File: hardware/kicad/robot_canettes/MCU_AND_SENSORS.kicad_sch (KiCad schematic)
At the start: 28 parts, among them J9 Conn_01x04_Pin, U1 STM32G431RBTx, U6 SN74AHCT1G125DBVR, Y1 16M

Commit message: Mise à jour de l'emplacement des composants
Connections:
- net GND: now also C1.2, C10.2, C15.2, C16.2, C17.2, C2.2, C22.2, C23.1, C3.2, C4.2, C5.2, C6.2, C7.2, C8.2, C9.2, H101.1, H102.1, H103.1, H104.1, J9.3 (Pin_3), LCSC1.11 (GNDDetect), LCSC1.5 (GND), LCSC1.7 (GND), R1.2, SW2.1, U1.15 (VSS), U1.27 (VSSA), U1.31 (VSS), U1.47 (VSS), U1.63 (VSS), Y1.2 (G), Y1.4 (G)
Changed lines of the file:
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@@
 			)
 		)
-		(property "Value" ""
+		(property "Value" "GND"
 			(at 52.07 91.44 0)
+			(hide yes)
 			(show_name no)
 			(do_not_autoplace no)
@@
 			)
 		)
-		(property "Value" ""
+		(property "Value" "GND"
 			(at 60.96 86.36 0)
+			(hide yes)
 			(show_name no)
 			(do_not_autoplace no)
@@
 			)
 		)
-		(property "Value" ""
+		(property "Value" "GND"
 			(at 113.03 166.37 0)
+			(hide yes)
 			(show_name no)
 			(do_not_autoplace no)
@@
 			)
 		)
-		(property "Value" ""
+		(property "Value" "GND"
 			(at 71.12 62.23 0)
+			(hide yes)
 			(show_name no)
 			(do_not_autoplace no)
@@
 			)
 		)
-		(property "Value" ""
+		(property "Value" "GND"
 			(at 248.92 52.07 0)
+			(hide yes)
 			(show_name no)
 			(do_not_autoplace no)
@@
 			)
 		)
-		(property "Value" ""
+		(property "Value" "GND"
 			(at 252.73 137.16 0)
+			(hide yes)
 			(show_name no)
 			(do_not_autoplace no)
@@
 			)
 		)
-		(property "Value" ""
+		(property "Value" "GND"
 			(at 64.77 101.6 0)
+			(hide yes)
 			(show_name no)
 			(do_not_autoplace no)
@@
 			)
 		)
-		(property "Value" ""
+		(property "Value" "GND"
 			(at 149.86 146.05 0)
+			(hide yes)
 			(show_name no)
 			(do_not_autoplace no)
@@
 			)
 		)
-		(property "Value" ""
+		(property "Value" "GND"
 			(at 52.07 181.61 0)
+			(hide yes)
 			(show_name no)
 			(do_not_autoplace no)
@@
 			)
 		)
-		(property "Value" ""
+		(property "Value" "GND"
 			(at 233.68 83.82 0)
+			(hide yes)
 			(show_name no)
 			(do_not_autoplace no)
@@
 			)
 		)
-		(property "Value" ""
+		(property "Value" "GND"
 			(at 243.84 137.16 0)
+			(hide yes)
 			(show_name no)
 			(do_not_autoplace no)
@@
 			)
 		)
-		(property "Value" ""
+		(property "Value" "GND"
 			(at 147.32 57.15 0)
+			(hide yes)
 			(show_name no)
 			(do_not_autoplace no)
@@
 			)
 		)
-		(property "Value" ""
+		(property "Value" "GND"
 			(at 45.72 80.01 0)
+			(hide yes)
 			(show_name no)
 			(do_not_autoplace no)

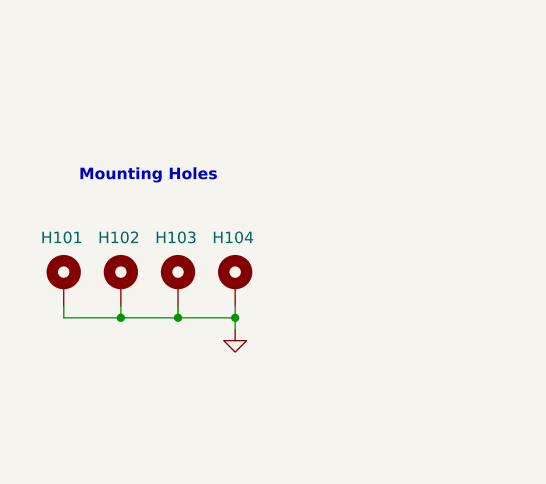
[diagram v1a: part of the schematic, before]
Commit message: Mise à jour PCB depuis le zip
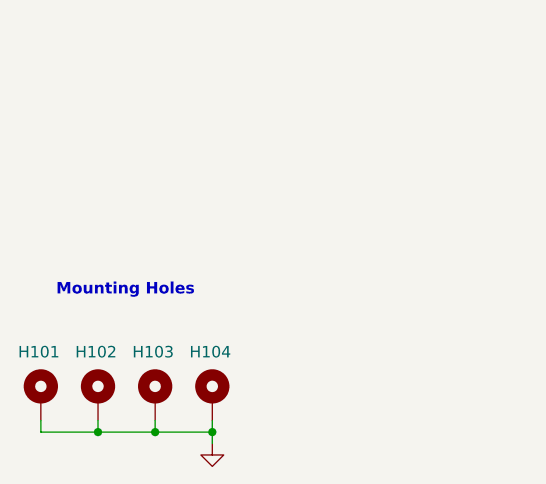
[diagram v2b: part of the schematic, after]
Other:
- moved on the sheet: H101, H102, H103, H104
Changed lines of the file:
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@@
 	(text "Mounting Holes"
 		(exclude_from_sim no)
-		(at 42.418 160.782 0)
+		(at 39.878 173.482 0)
 		(effects
 			(font
@@
 	)
 	(junction
-		(at 52.07 176.53)
+		(at 49.53 189.23)
 		(diameter 0)
 		(color 0 0 0 0)
 	)
 	(junction
-		(at 39.37 176.53)
+		(at 36.83 189.23)
 		(diameter 0)
 		(color 0 0 0 0)
@@
 	)
 	(junction
-		(at 45.72 176.53)
+		(at 43.18 189.23)
 		(diameter 0)
 		(color 0 0 0 0)
@@
 	(wire
 		(pts
-			(xy 45.72 176.53) (xy 39.37 176.53)
+			(xy 43.18 189.23) (xy 36.83 189.23)
 		)
 		(stroke
@@
 	(wire
 		(pts
-			(xy 33.02 176.53) (xy 33.02 175.26)
+			(xy 30.48 189.23) (xy 30.48 187.96)
 		)
 		(stroke
@@
 	(wire
 		(pts
-			(xy 39.37 176.53) (xy 39.37 175.26)
+			(xy 36.83 189.23) (xy 36.83 187.96)
 		)
 		(stroke
@@
 	(wire
 		(pts
-			(xy 39.37 176.53) (xy 33.02 176.53)
+			(xy 36.83 189.23) (xy 30.48 189.23)
 		)
 		(stroke
@@
 	(wire
 		(pts
-			(xy 52.07 176.53) (xy 52.07 177.8)
+			(xy 49.53 189.23) (xy 49.53 190.5)
 		)
 		(stroke
@@
 	(wire
 		(pts
-			(xy 52.07 175.26) (xy 52.07 176.53)
+			(xy 49.53 187.96) (xy 49.53 189.23)
 		)
 		(stroke
@@
 	(wire
 		(pts
-			(xy 52.07 176.53) (xy 45.72 176.53)
+			(xy 49.53 189.23) (xy 43.18 189.23)
 		)
 		(stroke
@@
 	(wire
 		(pts
-			(xy 45.72 176.53) (xy 45.72 175.26)
+			(xy 43.18 189.23) (xy 43.18 187.96)
 		)
 		(stroke
@@
 	(symbol
 		(lib_id "Mechanical:MountingHole_Pad")
-		(at 33.02 172.72 0)
+		(at 30.48 185.42 0)
 		(unit 1)
 		(body_style 1)
@@
 		(dnp no)
 		(property "Reference" "H101"
-			(at 30.48 167.64 0)
+			(at 27.94 180.34 0)
 			(show_name no)
 			(do_not_autoplace no)
@@
 		)
 		(property "Value" "MountingHole_Pad"
-			(at 35.56 172.72 0)
+			(at 33.02 185.42 0)
 			(hide yes)
 			(show_name no)
@@
 		)
 		(property "Footprint" "MountingHole:MountingHole_3.2mm_M3_Pad_Via"
-			(at 33.02 172.72 0)
+			(at 30.48 185.42 0)
 			(hide yes)
 			(show_name no)
@@
 		)
 		(property "Datasheet" ""
-			(at 33.02 172.72 0)
+			(at 30.48 185.42 0)
 			(hide yes)
 			(show_name no)
@@
 		)
 		(property "Description" ""
-			(at 33.02 172.72 0)
+			(at 30.48 185.42 0)
 			(show_name no)
 			(do_not_autoplace no)
@@
 	(symbol
 		(lib_id "Mechanical:MountingHole_Pad")
-		(at 39.37 172.72 0)
+		(at 36.83 185.42 0)
 		(unit 1)
 		(body_style 1)
@@
 		(dnp no)
 		(property "Reference" "H102"
-			(at 36.83 167.64 0)
+			(at 34.29 180.34 0)
 			(show_name no)
 			(do_not_autoplace no)
@@
 		)
 		(property "Value" "MountingHole_Pad"
-			(at 41.91 172.72 0)
+			(at 39.37 185.42 0)
 			(hide yes)
 			(show_name no)
@@
 		)
 		(property "Footprint" "MountingHole:MountingHole_3.2mm_M3_Pad_Via"
-			(at 39.37 172.72 0)
+			(at 36.83 185.42 0)
 			(hide yes)
 			(show_name no)
@@
 		)
 		(property "Datasheet" ""
-			(at 39.37 172.72 0)
+			(at 36.83 185.42 0)
 			(hide yes)
 			(show_name no)
@@
 		)
 		(property "Description" ""
-			(at 39.37 172.72 0)
+			(at 36.83 185.42 0)
 			(show_name no)
 			(do_not_autoplace no)
@@
 	(symbol
 		(lib_id "Mechanical:MountingHole_Pad")
-		(at 45.72 172.72 0)
+		(at 43.18 185.42 0)
 		(unit 1)
 		(body_style 1)
@@
 		(dnp no)
 		(property "Reference" "H103"
-			(at 43.18 167.64 0)
+			(at 40.64 180.34 0)
 			(show_name no)
 			(do_not_autoplace no)
@@
 		)
 		(property "Value" "MountingHole_Pad"
-			(at 48.26 172.72 0)
+			(at 45.72 185.42 0)
 			(hide yes)
 			(show_name no)
@@
 		)
 		(property "Footprint" "MountingHole:MountingHole_3.2mm_M3_Pad_Via"
-			(at 45.72 172.72 0)
+			(at 43.18 185.42 0)
 			(hide yes)
 			(show_name no)
@@
 		)
 		(property "Datasheet" ""
-			(at 45.72 172.72 0)
+			(at 43.18 185.42 0)
 			(hide yes)
 			(show_name no)
@@
 		)
 		(property "Description" ""
-			(at 45.72 172.72 0)
+			(at 43.18 185.42 0)
 			(show_name no)
 			(do_not_autoplace no)
@@
 		(lib_name "GND_14")
 		(lib_id "power:GND")
-		(at 52.07 177.8 0)
+		(at 49.53 190.5 0)
 		(unit 1)
 		(body_style 1)
@@
 		(dnp no)
 		(property "Reference" "#PWR0135"
-			(at 52.07 184.15 0)
+			(at 49.53 196.85 0)
 			(hide yes)
 			(show_name no)
@@
 		)
 		(property "Value" "GND"
-			(at 52.07 181.61 0)
+			(at 49.53 194.31 0)
 			(hide yes)
 			(show_name no)
@@
 		)
 		(property "Footprint" ""
-			(at 52.07 177.8 0)
+			(at 49.53 190.5 0)
 			(hide yes)
 			(show_name no)
@@
 		)
 		(property "Datasheet" ""
-			(at 52.07 177.8 0)
+			(at 49.53 190.5 0)
 			(hide yes)
 			(show_name no)
@@
 		)
 		(property "Description" ""
-			(at 52.07 177.8 0)
+			(at 49.53 190.5 0)
 			(show_name no)
 			(do_not_autoplace no)
@@
 	(symbol
 		(lib_id "Mechanical:MountingHole_Pad")
-		(at 52.07 172.72 0)
+		(at 49.53 185.42 0)
 		(unit 1)
 		(body_style 1)
@@
 		(dnp no)
 		(property "Reference" "H104"
-			(at 49.53 167.64 0)
+			(at 46.99 180.34 0)
 			(show_name no)
 			(do_not_autoplace no)
@@
 		)
 		(property "Value" "MountingHole_Pad"
-			(at 54.61 172.72 0)
+			(at 52.07 185.42 0)
 			(hide yes)
 			(show_name no)
@@
 		)
 		(property "Footprint" "MountingHole:MountingHole_3.2mm_M3_Pad_Via"
-			(at 52.07 172.72 0)
+			(at 49.53 185.42 0)
 			(hide yes)
 			(show_name no)
@@
 		)
 		(property "Datasheet" ""
-			(at 52.07 172.72 0)
+			(at 49.53 185.42 0)
 			(hide yes)
 			(show_name no)
@@
 		)
 		(property "Description" ""
-			(at 52.07 172.72 0)
+			(at 49.53 185.42 0)
 			(show_name no)
 			(do_not_autoplace no)

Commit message: Final PCB LAYOUT
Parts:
- J9: JLCPCB Part # C2691448 -> C131334
- U6: JLCPCB Part # C20617903 -> C7484
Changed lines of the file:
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@@
 			)
 		)
-		(property "JLCPCB Part #" "C2691448"
+		(property "JLCPCB Part #" "C131334"
 			(at 265.43 130.81 0)
 			(hide yes)
@@
 			)
 		)
-		(property "LCSC Part Number" ""
+		(property "JLCPCB Part #" "C7484"
 			(at 215.9 135.89 0)
 			(hide yes)
-			(show_name no)
-			(do_not_autoplace no)
-			(effects
-				(font
-					(size 1.27 1.27)
-				)
-			)
-		)
-		(property "LCSC Parts Number" ""
-			(at 215.9 135.89 0)
-			(hide yes)
-			(show_name no)
-			(do_not_autoplace no)
-			(effects
-				(font
-					(size 1.27 1.27)
-				)
-			)
-		)
-		(property "JLCPCB Part #" "C20617903"
-			(at 215.9 135.89 0)
-			(hide yes)

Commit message: Mise a jour des schemas, layout final, routage et génération des fichiers de fabrication de la carte
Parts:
- C1: JLCPCB PART# C15195 -> (none); JLCPCB Part # (none) -> C15195
- C10, C15, C22, C3, C6, C7, C8, C9: JLCPCB PART # C1525 -> (none); JLCPCB Part # (none) -> C1525
- C16, C17: JLCPCB PART # C123155 -> (none); JLCPCB Part # (none) -> C281766
- C2: JLCPCB PART # C141772 -> (none); JLCPCB Part # (none) -> C141772
- C4: JLCPCB Part # (none) -> C19666
- C5: #JLCPCB PART C1525 -> (none); JLCPCB Part # (none) -> C1525
- LCSC1: value C9900028921 -> (none); JLCPCB PART # C9900028921 -> (none); JLCPCB Part # (none) -> C3975190
- R1: JLCPCB PART # C174175 -> (none); JLCPCB Part # (none) -> C25744
- U1: JLCPCB PART # C431633 -> (none); JLCPCB Part # (none) -> C431633
- Y1: JLCPCB PART # C13738 -> (none); JLCPCB Part # (none) -> C13738; private KLC_S4.1 -> KLC_S3.3
- renumbered J9 to NEOPIXEL1
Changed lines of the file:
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@@
 		(dnp no)
 		(property "Reference" "C5"
-			(at 81.28 49.5299 0)
-			(hide yes)
+			(at 75.438 48.768 0)
 			(show_name no)
 			(do_not_autoplace no)
@@
 			)
 		)
-		(property "#JLCPCB PART" "C1525"
+		(property "JLCPCB Part #" "C1525"
 			(at 78.74 50.8 0)
 			(hide yes)
@@
 			)
 		)
-		(property "JLCPCB PART#" "C15195"
+		(property "JLCPCB Part #" "C15195"
 			(at 134.62 46.99 0)
 			(hide yes)
@@
 			)
 		)
-		(property "JLCPCB PART #" "C1525"
+		(property "JLCPCB Part #" "C1525"
 			(at 60.96 77.47 0)
 			(hide yes)
@@
 			)
 		)
-		(property "JLCPCB PART #" "C1525"
+		(property "JLCPCB Part #" "C1525"
 			(at 45.72 72.39 0)
 			(hide yes)
@@
 		(dnp no)
 		(property "Reference" "C7"
-			(at 91.44 49.5299 0)
-			(hide yes)
+			(at 86.106 48.768 0)
 			(show_name no)
 			(do_not_autoplace no)
@@
 			)
 		)
-		(property "JLCPCB PART #" "C1525"
+		(property "JLCPCB Part #" "C1525"
 			(at 88.9 50.8 0)
 			(hide yes)
@@
 			)
 		)
-		(property "JLCPCB PART #" "C123155"
+		(property "JLCPCB Part #" "C281766"
 			(at 81.28 91.44 0)
 			(hide yes)
@@
 			)
 		)
-		(property "Value" "C9900028921"
+		(property "Value" ""
 			(at 242.57 57.1501 0)
 			(show_name no)
@@
 			)
 		)
-		(property "JLCPCB PART #" "C9900028921"
+		(property "JLCPCB Part #" "C3975190"
 			(at 231.14 58.42 0)
 			(hide yes)
@@
 			)
 		)
-		(property "JLCPCB PART #" "C141772"
+		(property "JLCPCB Part #" "C141772"
 			(at 128.27 46.99 0)
 			(hide yes)
@@
 			)
 		)
-		(property "JLCPCB PART #" "C174175"
+		(property "JLCPCB Part #" "C25744"
 			(at 149.86 137.16 0)
 			(hide yes)
@@
 			)
 		)
-		(property "JLCPCB PART #" "C123155"
+		(property "JLCPCB Part #" "C281766"
 			(at 64.77 90.17 0)
 			(hide yes)
@@
 		(in_pos_files yes)
 		(dnp no)
-		(property "Reference" "J9"
+		(property "Reference" "NEOPIXEL1"
 			(at 264.795 123.19 0)
 			(show_name no)
@@
 			(project "robot_canettes"
 				(path "/67ea9330-6bd8-4bfd-bb5f-e77247705b59/3f58a58d-8204-4b17-9646-a60f600133ec"
-					(reference "J9")
+					(reference "NEOPIXEL1")
 					(unit 1)
 				)
@@
 		(dnp no)
 		(property "Reference" "C22"
-			(at 244.602 42.672 0)
+			(at 243.078 41.91 0)
 			(show_name no)
 			(do_not_autoplace no)
@@
 			)
 		)
-		(property "JLCPCB PART #" "C1525"
+		(property "JLCPCB Part #" "C1525"
 			(at 248.92 43.18 0)
 			(hide yes)
@@
 		(dnp no)
 		(property "Reference" "C6"
-			(at 86.36 49.5299 0)
-			(hide yes)
+			(at 80.772 48.768 0)
 			(show_name no)
 			(do_not_autoplace no)
@@
 			)
 		)
-		(property "JLCPCB PART #" "C1525"
+		(property "JLCPCB Part #" "C1525"
 			(at 83.82 50.8 0)
 			(hide yes)
@@
 		(dnp no)
 		(property "Reference" "C8"
-			(at 96.52 49.5299 0)
-			(hide yes)
+			(at 91.186 48.768 0)
 			(show_name no)
 			(do_not_autoplace no)
@@
 			)
 		)
-		(property "JLCPCB PART #" "C1525"
+		(property "JLCPCB Part #" "C1525"
 			(at 93.98 50.8 0)
 			(hide yes)
@@
 		(dnp no)
 		(property "Reference" "C9"
-			(at 101.6 49.5299 0)
-			(hide yes)
+			(at 96.266 48.768 0)
 			(show_name no)
 			(do_not_autoplace no)
@@
 			)
 		)
-		(property "JLCPCB PART #" "C1525"
+		(property "JLCPCB Part #" "C1525"
 			(at 99.06 50.8 0)
 			(hide yes)
@@
 			)
 		)
-		(property private "KLC_S4.1" "Some pins are on 50mil grid to make the symbol small"
-			(at 63.5 83.82 0)
-			(hide yes)
-			(show_name yes)
-			(do_not_autoplace no)
-			(effects
-				(font
-					(size 1.27 1.27)
-				)
-			)
-		)
-		(property "JLCPCB PART #" "C13738"
+		(property "JLCPCB Part #" "C13738"
 			(at 78.74 83.82 90)
 			(hide yes)
@@
 			)
 		)
-		(property "JLCPCB PART #" " C431633 "
+		(property "JLCPCB Part #" " C431633 "
 			(at 111.76 110.49 0)
 			(hide yes)
@@
 			)
 		)
+		(property "JLCPCB Part #" "C19666"
+			(at 104.14 50.8 0)
+			(hide yes)
+			(show_name no)
+			(do_not_autoplace no)
+			(effects
+				(font
+					(size 1.27 1.27)
+				)
+			)
+		)
 		(pin "1"
 		)
@@
 			)
 		)
-		(property "JLCPCB PART #" "C1525"
+		(property "JLCPCB Part #" "C1525"
 			(at 140.97 46.99 0)
 			(hide yes)
